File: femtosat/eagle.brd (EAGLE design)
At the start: 21 x 59.1 mm, 23 parts, among them U1 ATMEGA328P_TQFP, U2 915MHz, U3 3.3V/150mA, U4 9DoF IMU, U5 BME280, Y1 16MHz

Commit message: Final Checkoff
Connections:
- net GND: now also J2.2; no longer J2.1
- net N$4: now also J2.1; no longer J2.2
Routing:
- net GND: track 166.8 -> 171.6 mm
- net 3.3V: track 81.0 -> 85.1 mm
- net N$4: track 6.81 -> 8.04 mm
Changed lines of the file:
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@@
 <wire x1="17.78" y1="71.755" x2="20.955" y2="67.945" width="0.254" layer="20"/>
 <wire x1="20.955" y1="67.945" x2="20.955" y2="12.7" width="0.254" layer="20"/>
-<hole x="10.541" y="68.58" drill="5.0038"/>
-<text x="5.08" y="63.754" size="1.778" layer="21" font="fixed">Angstrom</text>
+<hole x="10.668" y="68.072" drill="5.0038"/>
+<text x="5.08" y="63.627" size="1.778" layer="21" font="fixed">Angstrom</text>
 <text x="0.762" y="42.672" size="1.27" layer="21" font="fixed">SCL</text>
 <text x="0.635" y="38.1" size="1.27" layer="21" font="fixed">SDA</text>
@@
 <wire x1="19.1008" y1="60.96" x2="19.5072" y2="60.96" width="0.254" layer="1"/>
 <wire x1="18.288" y1="61.7728" x2="19.1008" y2="60.96" width="0.254" layer="1"/>
-<wire x1="11.5824" y1="61.7728" x2="9.7536" y2="61.7728" width="0.254" layer="1"/>
+<wire x1="11.5824" y1="61.7728" x2="5.8928" y2="61.7728" width="0.254" layer="1"/>
 <wire x1="11.5824" y1="61.7728" x2="18.288" y2="61.7728" width="0.254" layer="1"/>
 <wire x1="19.5072" y1="60.96" x2="19.546" y2="60.96" width="0.254" layer="1"/>
@@
 <wire x1="6.985" y1="49.53" x2="7.62" y2="48.895" width="0.254" layer="1"/>
 <wire x1="7.62" y1="48.895" x2="8.89" y2="48.895" width="0.254" layer="1"/>
-<wire x1="8.925" y1="49.681" x2="8.925" y2="48.93" width="0.254" layer="1"/>
+<wire x1="8.925" y1="49.681" x2="8.925" y2="48.93" width="0.1524" layer="1"/>
 <wire x1="8.925" y1="48.93" x2="8.89" y2="48.895" width="0.254" layer="1"/>
 <wire x1="4.23" y1="51.435" x2="4.23" y2="53.125" width="0.254" layer="1"/>
 <wire x1="4.23" y1="53.125" x2="5.08" y2="53.975" width="0.254" layer="1"/>
 <wire x1="5.08" y1="53.975" x2="5.08" y2="55.88" width="0.254" layer="1"/>
-<wire x1="3.81" y1="57.15" x2="3.81" y2="58.42" width="0.254" layer="1"/>
-<wire x1="3.81" y1="58.42" x2="4.81" y2="59.42" width="0.254" layer="1"/>
-<wire x1="5.08" y1="55.88" x2="3.81" y2="57.15" width="0.254" layer="1"/>
 <wire x1="2.794" y1="35.433" x2="1.143" y2="35.433" width="0.254" layer="1"/>
 <wire x1="1.143" y1="35.433" x2="0.635" y2="34.925" width="0.254" layer="1"/>
@@
 <wire x1="3.041" y1="21.003" x2="2.993" y2="20.955" width="0.254" layer="1"/>
 <wire x1="2.993" y1="20.955" x2="0.8128" y2="20.955" width="0.254" layer="1"/>
-<contactref element="J2" pad="1"/>
 <contactref element="U3" pad="2"/>
 <contactref element="C1" pad="2"/>
-<wire x1="4.81" y1="59.42" x2="7.51" y2="59.42" width="0.254" layer="1"/>
-<wire x1="9.725" y1="52.681" x2="9.725" y2="54.175" width="0.254" layer="1"/>
+<wire x1="9.725" y1="52.681" x2="9.725" y2="54.175" width="0.1524" layer="1"/>
 <wire x1="9.725" y1="54.175" x2="10.795" y2="55.245" width="0.254" layer="1"/>
 <wire x1="10.795" y1="55.245" x2="13.081" y2="55.245" width="0.254" layer="1"/>
 <wire x1="13.081" y1="55.245" x2="13.208" y2="55.245" width="0.254" layer="1"/>
 <wire x1="19.646" y1="58.547" x2="19.646" y2="56.388" width="0.254" layer="1"/>
-<wire x1="9.7536" y1="61.7728" x2="7.51" y2="59.5292" width="0.254" layer="1"/>
-<wire x1="7.51" y1="59.5292" x2="7.51" y2="59.42" width="0.254" layer="1"/>
 <wire x1="13.0048" y1="58.1152" x2="12.6746" y2="57.785" width="0.254" layer="1"/>
 <wire x1="12.6746" y1="57.785" x2="12.0349" y2="57.785" width="0.254" layer="1"/>
@@
 <wire x1="13.503" y1="52.206" x2="13.503" y2="51.9274" width="0.254" layer="1"/>
 <wire x1="13.503" y1="51.9274" x2="14.0208" y2="51.4096" width="0.254" layer="1"/>
-<wire x1="7.9725" y1="50.181" x2="7.001" y2="50.181" width="0.254" layer="1"/>
+<wire x1="7.9725" y1="50.181" x2="7.001" y2="50.181" width="0.1524" layer="1"/>
 <wire x1="7.001" y1="50.181" x2="6.985" y2="50.165" width="0.254" layer="1"/>
 <wire x1="6.985" y1="50.165" x2="4.2672" y2="50.165" width="0.254" layer="1"/>
-<wire x1="8.925" y1="52.681" x2="8.89" y2="52.716" width="0.254" layer="1"/>
-<wire x1="8.89" y1="52.716" x2="8.89" y2="53.34" width="0.254" layer="1"/>
 <polygon width="0.1524" layer="1" isolate="0.254">
 <vertex x="0" y="15.875"/>
@@
 <vertex x="17.78" y="71.755"/>
 </polygon>
+<contactref element="J2" pad="2"/>
+<wire x1="5.08" y1="55.88" x2="6.62" y2="57.42" width="0.254" layer="1"/>
+<wire x1="6.62" y1="57.42" x2="7.51" y2="57.42" width="0.254" layer="1"/>
+<wire x1="5.8928" y1="61.7728" x2="3.81" y2="59.69" width="0.254" layer="1"/>
+<wire x1="3.81" y1="59.69" x2="3.81" y2="58.42" width="0.254" layer="1"/>
+<wire x1="3.81" y1="58.42" x2="4.81" y2="57.42" width="0.254" layer="1"/>
+<wire x1="4.81" y1="57.42" x2="7.51" y2="57.42" width="0.254" layer="1"/>
+<wire x1="8.925" y1="52.681" x2="8.89" y2="52.716" width="0.1524" layer="1"/>
+<wire x1="8.89" y1="52.716" x2="8.89" y2="53.34" width="0.1524" layer="1"/>
 </signal>
 <signal name="N$5">
@@
 <wire x1="14.4272" y1="46.736" x2="14.478" y2="46.736" width="0.254" layer="16"/>
 <via x="14.4272" y="42.672" extent="1-16" drill="0.3302"/>
-<wire x1="7.9725" y1="52.181" x2="8.779" y2="52.181" width="0.254" layer="1"/>
-<wire x1="8.779" y1="52.181" x2="9.525" y2="51.435" width="0.254" layer="1"/>
-<wire x1="9.525" y1="51.435" x2="10.125" y2="52.035" width="0.254" layer="1"/>
-<wire x1="10.125" y1="52.035" x2="10.125" y2="52.681" width="0.254" layer="1"/>
-<wire x1="11.0775" y1="50.181" x2="10.779" y2="50.181" width="0.254" layer="1"/>
-<wire x1="10.779" y1="50.181" x2="9.525" y2="51.435" width="0.254" layer="1"/>
-<wire x1="11.0775" y1="50.181" x2="13.478" y2="50.181" width="0.254" layer="1"/>
+<wire x1="10.125" y1="52.035" x2="9.525" y2="51.435" width="0.1524" layer="1"/>
+<wire x1="10.125" y1="52.035" x2="10.125" y2="52.681" width="0.1524" layer="1"/>
+<wire x1="11.0775" y1="50.181" x2="12.065" y2="50.181" width="0.1524" layer="1"/>
+<wire x1="12.065" y1="50.181" x2="13.478" y2="50.181" width="0.1524" layer="1"/>
 <wire x1="13.478" y1="50.181" x2="13.503" y2="50.156" width="0.254" layer="1"/>
+<wire x1="7.9725" y1="52.181" x2="8.398" y2="52.181" width="0.1524" layer="1"/>
+<wire x1="9.144" y1="51.435" x2="9.525" y2="51.435" width="0.1524" layer="1"/>
+<wire x1="8.398" y1="52.181" x2="9.144" y2="51.435" width="0.1524" layer="1"/>
+<wire x1="10.125" y1="52.681" x2="10.125" y2="53.305" width="0.1524" layer="1"/>
+<wire x1="10.125" y1="53.305" x2="10.668" y2="53.848" width="0.1524" layer="1"/>
+<wire x1="10.668" y1="53.848" x2="11.557" y2="53.848" width="0.1524" layer="1"/>
+<wire x1="11.557" y1="53.848" x2="12.065" y2="53.34" width="0.1524" layer="1"/>
+<wire x1="12.065" y1="53.34" x2="12.065" y2="50.181" width="0.1524" layer="1"/>
 </signal>
 <signal name="INT">
@@
 <contactref element="U3" pad="1"/>
 <contactref element="U3" pad="3"/>
-<contactref element="J2" pad="2"/>
 <wire x1="11.5824" y1="56.896" x2="11.9888" y2="56.896" width="0.254" layer="1"/>
 <wire x1="10.9728" y1="57.5056" x2="11.5824" y2="56.896" width="0.254" layer="1"/>
@@
 <wire x1="11.9888" y1="56.896" x2="12.0349" y2="56.835" width="0.254" layer="1"/>
 <wire x1="11.9888" y1="58.7248" x2="12.0349" y2="58.735" width="0.254" layer="1"/>
-<wire x1="7.5184" y1="57.5056" x2="10.9728" y2="57.5056" width="0.254" layer="1"/>
-<wire x1="7.5184" y1="57.5056" x2="7.51" y2="57.42" width="0.254" layer="1"/>
+<contactref element="J2" pad="1"/>
+<wire x1="7.51" y1="59.42" x2="11.2936" y2="59.42" width="0.254" layer="1"/>
+<wire x1="11.2936" y1="59.42" x2="11.9888" y2="58.7248" width="0.254" layer="1"/>
 </signal>
 <signal name="N$7">
@@
 <via x="11.9888" y="42.0624" extent="1-16" drill="0.3302"/>
 <via x="4.064" y="46.1264" extent="1-16" drill="0.3302"/>
-<wire x1="10.525" y1="49.6285" x2="10.525" y2="49.165" width="0.254" layer="1"/>
-<wire x1="11.43" y1="48.26" x2="12.065" y2="48.26" width="0.254" layer="1"/>
+<wire x1="10.525" y1="49.6285" x2="10.525" y2="49.165" width="0.1524" layer="1"/>
+<wire x1="11.43" y1="48.26" x2="12.065" y2="48.26" width="0.1524" layer="1"/>
 <via x="12.065" y="48.26" extent="1-16" drill="0.35"/>
 <wire x1="12.065" y1="48.26" x2="12.065" y2="48.895" width="0.254" layer="16"/>
 <wire x1="12.065" y1="48.895" x2="11.8872" y2="49.0728" width="0.254" layer="16"/>
-<wire x1="10.525" y1="49.165" x2="11.43" y2="48.26" width="0.254" layer="1"/>
+<wire x1="10.525" y1="49.165" x2="11.43" y2="48.26" width="0.1524" layer="1"/>
 <wire x1="3.39" y1="45.085" x2="4.445" y2="43.18" width="0.254" layer="1"/>
 </signal>
@@
 <via x="10.9728" y="42.0624" extent="1-16" drill="0.3302"/>
 <via x="2.6416" y="42.4688" extent="1-16" drill="0.3302"/>
-<wire x1="10.125" y1="49.681" x2="10.125" y2="48.549" width="0.254" layer="1"/>
-<wire x1="10.125" y1="48.549" x2="11.938" y2="46.736" width="0.254" layer="1"/>
+<wire x1="10.125" y1="49.681" x2="10.125" y2="48.549" width="0.1524" layer="1"/>
+<wire x1="10.125" y1="48.549" x2="11.938" y2="46.736" width="0.1524" layer="1"/>
 <wire x1="3.39" y1="41.275" x2="4.445" y2="41.275" width="0.254" layer="1"/>
 <wire x1="4.445" y1="41.275" x2="4.445" y2="38.735" width="0.254" layer="1"/>
@@
 <contactref element="U4" pad="10"/>
 <contactref element="C5" pad="2"/>
-<wire x1="9.325" y1="52.681" x2="9.325" y2="53.54" width="0.254" layer="1"/>
-<wire x1="9.325" y1="53.54" x2="8.89" y2="53.975" width="0.254" layer="1"/>
-<wire x1="8.89" y1="53.975" x2="6.985" y2="53.975" width="0.254" layer="1"/>
-<wire x1="5.93" y1="52.92" x2="5.93" y2="51.435" width="0.254" layer="1"/>
-<wire x1="6.985" y1="53.975" x2="5.93" y2="52.92" width="0.254" layer="1"/>
+<wire x1="9.325" y1="52.681" x2="9.325" y2="53.54" width="0.1524" layer="1"/>
+<wire x1="9.325" y1="53.54" x2="8.89" y2="53.975" width="0.1524" layer="1"/>
+<wire x1="8.89" y1="53.975" x2="6.985" y2="53.975" width="0.1524" layer="1"/>
+<wire x1="5.93" y1="52.92" x2="5.93" y2="51.435" width="0.1524" layer="1"/>
+<wire x1="6.985" y1="53.975" x2="5.93" y2="52.92" width="0.1524" layer="1"/>
 </signal>
 </signals>

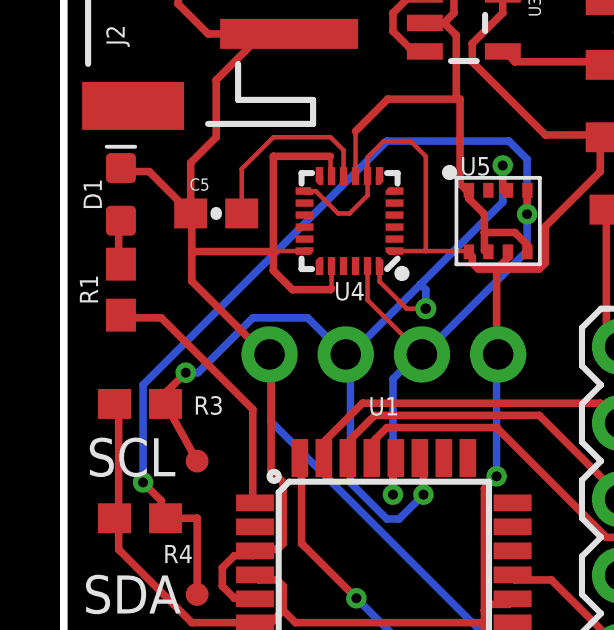
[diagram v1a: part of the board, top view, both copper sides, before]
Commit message: Added backside Silkscreen
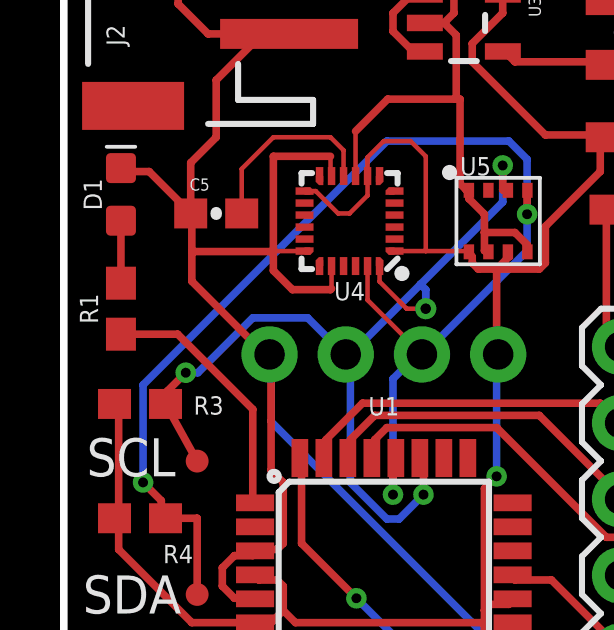
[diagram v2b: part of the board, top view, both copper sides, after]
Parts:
- moved R1 0.64 mm to (1.91, 48.3)
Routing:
- net N$12: track 1.51 -> 2.37 mm
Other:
- board text added: "Autumn 2019"
- board text added: "BYU"
- board text added: "DTR"
- board text added: "GND"
- board text added: "RXI"
- board text added: "TXO"
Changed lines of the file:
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@@
 <text x="0.762" y="42.672" size="1.27" layer="21" font="fixed">SCL</text>
 <text x="0.635" y="38.1" size="1.27" layer="21" font="fixed">SDA</text>
+<text x="12.7" y="17.78" size="1.778" layer="22" font="fixed" rot="MR0">BYU</text>
+<text x="15.24" y="16.51" size="1.016" layer="22" font="fixed" rot="MR0">Autumn 2019</text>
+<text x="17.272" y="43.053" size="1.016" layer="22" font="fixed" rot="MR315">TXO</text>
+<text x="17.272" y="40.513" size="1.016" layer="22" font="fixed" rot="MR315">RXI</text>
+<text x="17.145" y="45.593" size="1.016" layer="22" font="fixed" rot="MR315">DTR</text>
+<text x="17.272" y="35.56" size="1.016" layer="22" font="fixed" rot="MR315">GND</text>
 </plain>
 <attributes>
@@
 <attribute name="VALUE" x="21.717" y="33.02" size="1.27" layer="27" rot="R90"/>
 </element>
-<element name="R1" library="femtosat" package="0603" value="330" x="1.905" y="48.895" smashed="yes" rot="R90">
-<attribute name="DIGIKEY" value="311-330GRCT-ND " x="59.055" y="67.945" size="1.778" layer="27" rot="R90" display="off"/>
-<attribute name="NAME" x="1.143" y="48.895" size="0.6096" layer="25" font="vector" ratio="20" rot="R90" align="bottom-center"/>
-<attribute name="VALUE" x="2.667" y="48.895" size="0.6096" layer="27" font="vector" ratio="20" rot="R90" align="top-center"/>
+<element name="R1" library="femtosat" package="0603" value="330" x="1.905" y="48.26" smashed="yes" rot="R90">
+<attribute name="DIGIKEY" value="311-330GRCT-ND " x="59.055" y="67.31" size="1.778" layer="27" rot="R90" display="off"/>
+<attribute name="NAME" x="1.143" y="48.26" size="0.6096" layer="25" font="vector" ratio="20" rot="R90" align="bottom-center"/>
+<attribute name="VALUE" x="2.667" y="48.26" size="0.6096" layer="27" font="vector" ratio="20" rot="R90" align="top-center"/>
 </element>
 <element name="R2" library="femtosat" package="0603-RES" value="10K" x="18.796" y="53.975" smashed="yes" rot="R180">
@@
 <contactref element="U1" pad="1"/>
 <contactref element="R1" pad="1"/>
-<wire x1="3.2512" y1="47.9552" x2="2.032" y2="47.9552" width="0.254" layer="1"/>
-<wire x1="6.2992" y1="44.9072" x2="3.2512" y2="47.9552" width="0.254" layer="1"/>
 <wire x1="6.2992" y1="41.8592" x2="6.2992" y2="44.9072" width="0.254" layer="1"/>
-<wire x1="2.032" y1="47.9552" x2="1.905" y2="48.045" width="0.254" layer="1"/>
 <wire x1="6.2992" y1="41.8592" x2="6.3754" y2="41.789" width="0.254" layer="1"/>
+<wire x1="3.7964" y1="47.41" x2="1.905" y2="47.41" width="0.254" layer="1"/>
+<wire x1="6.2992" y1="44.9072" x2="3.7964" y2="47.41" width="0.254" layer="1"/>
 </signal>
 <signal name="N$12">
 <contactref element="R1" pad="2"/>
 <contactref element="D1" pad="A"/>
-<wire x1="1.8288" y1="49.784" x2="1.8288" y2="51.0032" width="0.254" layer="1"/>
 <wire x1="1.8288" y1="51.0032" x2="1.905" y2="51.193" width="0.254" layer="1"/>
-<wire x1="1.8288" y1="49.784" x2="1.905" y2="49.745" width="0.254" layer="1"/>
+<wire x1="1.8288" y1="49.149" x2="1.905" y2="49.11" width="0.254" layer="1"/>
+<wire x1="1.905" y1="51.193" x2="1.905" y2="49.2252" width="0.254" layer="1"/>
+<wire x1="1.905" y1="49.2252" x2="1.8288" y2="49.149" width="0.254" layer="1"/>
 </signal>
 <signal name="N$14">
